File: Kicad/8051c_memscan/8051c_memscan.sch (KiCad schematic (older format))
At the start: 15 parts, among them J1 Conn_01x14_Male, SW1 SW_DPST_x2, U1 AT89C2051-12PU, Y1 4-12Mhz

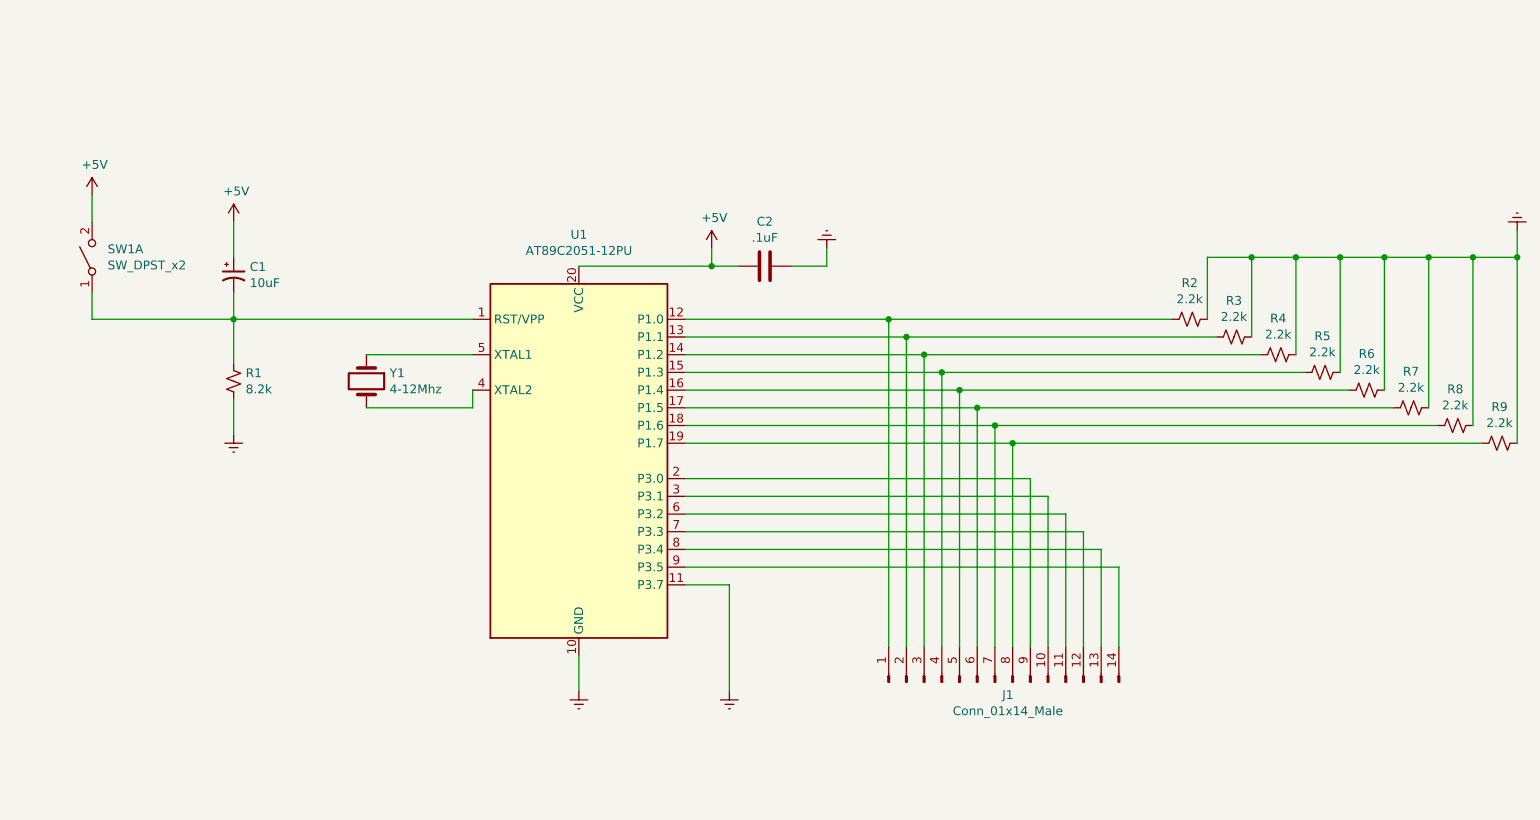
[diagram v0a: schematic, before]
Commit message: Folding in feedback and using correct symbol footprint: https://www.snapeda.com/parts/P80C51FA-4N%2C112/NXP%20USA%20Inc./view-part/?ref=search&t=80c51
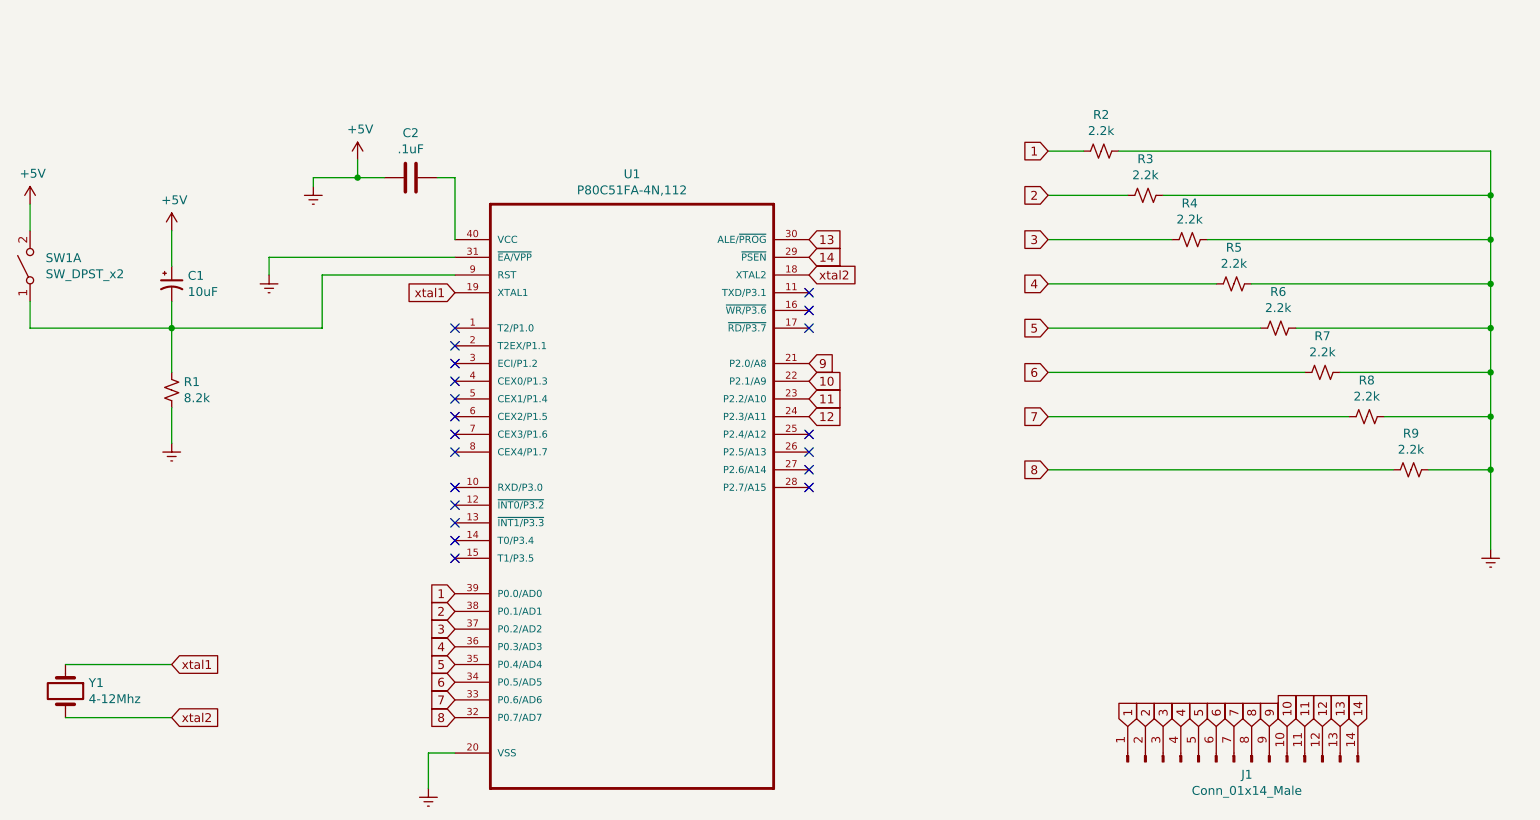
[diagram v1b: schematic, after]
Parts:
- removed U1: AT89C2051-12PU, Package_DIP:DIP-20_W7.62mm, symbol MCU_Microchip_8051:AT89C2051-12PU
- added U1: P80C51FA-4N,112, DIP254P1524X470-40, symbol P80C51FA-4N_112:P80C51FA-4N,112
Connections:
- net +5V: now also R1.2, R2.1, R3.1, R4.1, R5.1, R6.1, R7.1, R8.1, R9.1, U1.20 (VSS), U1.31 (~EA/VPP)
- net at C1.2, R1.1, SW1.1 (A): now also U1.9 (RST)
- net 1: now reaches J1.1 (Pin_1), R2.2
- net 1: now also U1.39 (P0.0/AD0)
- net 2: now reaches J1.2 (Pin_2), R3.2
- net 2: now also U1.38 (P0.1/AD1)
- net 3: now reaches J1.3 (Pin_3), R4.2
- net 3: now also U1.37 (P0.2/AD2)
- net 4: now reaches J1.4 (Pin_4), R5.2
- net 4: now also U1.36 (P0.3/AD3)
- net 5: now reaches J1.5 (Pin_5), R6.2
- net 5: now also U1.35 (P0.4/AD4)
- net 6: now reaches J1.6 (Pin_6), R7.2
- net 6: now also U1.34 (P0.5/AD5)
- net 7: now reaches J1.7 (Pin_7), R8.2
- net 7: now also U1.33 (P0.6/AD6)
- net 8: now reaches J1.8 (Pin_8), R9.2
- net 8: now also U1.32 (P0.7/AD7)
- net 9: now reaches J1.9 (Pin_9)
- net 9: now also U1.21 (P2.0/A8)
- net 10: now reaches J1.10 (Pin_10)
- net 10: now also U1.22 (P2.1/A9)
- net xtal2: now reaches Y1.2
- net xtal2: now also U1.18 (XTAL2)
- net xtal1: now reaches Y1.1
- net xtal1: now also U1.19 (XTAL1)
- net 11: now reaches J1.11 (Pin_11)
- net 11: now also U1.23 (P2.2/A10)
- net 12: now reaches J1.12 (Pin_12)
- net 12: now also U1.24 (P2.3/A11)
- net 13: now reaches J1.13 (Pin_13)
- net 13: now also U1.30 (ALE/~PROG)
- net 14: now reaches J1.14 (Pin_14)
- net 14: now also U1.29 (~PSEN)
- removed net Earth: C2.2, R1.2, R2.1, R3.1, R4.1, R5.1, R6.1, R7.1, R8.1, R9.1
- new net: C2.2, U1.40 (VCC)
- no-connect marks 0 -> 20
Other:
- moved on the sheet: C1, C2, J1, R1, SW1A, Y1

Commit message: Added power connector pins.
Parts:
- added J2: Conn_01x02_Male, symbol Connector:Conn_01x02_Male
- U1: symbol P80C51FA-4N_112:P80C51FA-4N,112 -> 8051c_memscan-rescue:P80C51FA-4N,112-P80C51FA-4N_112
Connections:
- net +5V: now also J2.1 (Pin_1), J2.2 (Pin_2)
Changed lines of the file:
@@
 EESchema Schematic File Version 4
 LIBS:8051c_memscan-cache
-EELAYER 26 0
+EELAYER 29 0
 EELAYER END
 $Descr A4 11693 8268
@@
 	3500 1900 3650 1900
 $Comp
-L P80C51FA-4N_112:P80C51FA-4N,112 U1
+L 8051c_memscan-rescue:P80C51FA-4N,112-P80C51FA-4N_112 U1
 U 1 1 5D70DC40
 P 5050 3550
@@
 Text GLabel 7400 3550 0    50   Input ~ 0
 8
+$Comp
+L Connector:Conn_01x02_Male J2
+U 1 1 5D70B128
+P 2200 1250
+F 0 "J2" H 2308 1431 50  0000 C CNN
+F 1 "Conn_01x02_Male" H 2308 1340 50  0000 C CNN
+F 2 "" H 2200 1250 50  0001 C CNN
+F 3 "~" H 2200 1250 50  0001 C CNN
+	1    2200 1250
+	1    0    0    -1
+$EndComp
+$Comp
+L power:+5V #PWR010
+U 1 1 5D70C5D4
+P 2900 1200
+F 0 "#PWR010" H 2900 1050 50  0001 C CNN
+F 1 "+5V" H 2915 1373 50  0000 C CNN
+F 2 "" H 2900 1200 50  0001 C CNN
+F 3 "" H 2900 1200 50  0001 C CNN
+	1    2900 1200
+	1    0    0    -1
+$EndComp
+$Comp
+L power:Earth #PWR09
+U 1 1 5D70CF88
+P 2650 1400
+F 0 "#PWR09" H 2650 1150 50  0001 C CNN
+F 1 "Earth" H 2650 1250 50  0001 C CNN
+F 2 "" H 2650 1400 50  0001 C CNN
+F 3 "~" H 2650 1400 50  0001 C CNN
+	1    2650 1400
+	1    0    0    -1
+$EndComp
+Wire Wire Line
+	2400 1250 2900 1250
+Wire Wire Line
+	2900 1250 2900 1200
+Wire Wire Line
+	2400 1350 2650 1350
+Wire Wire Line
+	2650 1350 2650 1400
 $EndSCHEMATC
